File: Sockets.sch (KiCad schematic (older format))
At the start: 55 parts, among them J10 CA58SUB-B, J11 PC6 EPSON MAINBOARD, J12 Y AXIS, J13 Z AXIS, J14 LED 1, J15 LED 2, J6 LIMIT Y BACK, J7 LIMIT Y FRONT, J8 LIMIT Z UP, J9 LIMIT Z DOWN, Q1 2N7002K, Q2 2N7002K, Q3 2N7002K, Q4 2N7002K, Q5 2N7002K, Q6 2N7002K, Q7 2N7002K, U5 74HC245

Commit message: Routing almost finished
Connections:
- net LED1_CNT: now also RN1.1 (R1.1); no longer RN2.4 (R4.1)
- net LED1_CONTROL: now also U5.5 (A3); no longer U5.6 (A4)
- net LED2_CNT: now also RN1.2 (R2.1); no longer RN2.3 (R3.1)
- net LED2_CONTROL: now also U5.4 (A2); no longer U5.7 (A5)
- net SPI_MOSI: now also U5.2 (A0); no longer U5.8 (A6)
- net SPI_MOSI_BUF: now also RN1.4 (R4.1); no longer RN2.2 (R2.1)
- net SPI_SCLK: now also U5.3 (A1); no longer U5.9 (A7)
- net SPI_SCLK_BUF: now also RN1.3 (R3.1); no longer RN2.1 (R1.1)
- net YDIR: now also RN2.2 (R2.1); no longer RN1.3 (R3.1)
- net YSTEP: now also RN2.1 (R1.1); no longer RN1.4 (R4.1)
- net Y_DIR: now also U5.8 (A6); no longer U5.3 (A1)
- net Y_STEP: now also U5.9 (A7); no longer U5.2 (A0)
- net ZDIR: now also RN2.4 (R4.1); no longer RN1.1 (R1.1)
- net ZSTEP: now also RN2.3 (R3.1); no longer RN1.2 (R2.1)
- net Z_DIR: now also U5.6 (A4); no longer U5.5 (A3)
- net Z_STEP: now also U5.7 (A5); no longer U5.4 (A2)
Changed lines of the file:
@@
 Text Notes 4550 2600 0    50   ~ 0
 PE Signal Output to Emulate PE Sensor
-Text GLabel 4700 5600 0    50   Input ~ 0
+Text GLabel 4700 6300 0    50   Input ~ 0
 Y_STEP
-Text GLabel 4700 5700 0    50   Input ~ 0
+Text GLabel 4700 6200 0    50   Input ~ 0
 Y_DIR
+Text GLabel 4700 6100 0    50   Input ~ 0
+Z_STEP
+Text GLabel 4700 6000 0    50   Input ~ 0
+Z_DIR
+Text GLabel 4700 5900 0    50   Input ~ 0
+LED1_CONTROL
 Text GLabel 4700 5800 0    50   Input ~ 0
-Z_STEP
-Text GLabel 4700 5900 0    50   Input ~ 0
-Z_DIR
-Text GLabel 4700 6000 0    50   Input ~ 0
-LED1_CONTROL
-Text GLabel 4700 6100 0    50   Input ~ 0
 LED2_CONTROL
 $Comp
@@
 Wire Wire Line
 	4550 6500 4700 6500
-Text Label 6550 5600 2    50   ~ 0
+Text Label 6550 6300 2    50   ~ 0
 YSTEP
-Text Label 6550 5700 2    50   ~ 0
+Text Label 6550 6200 2    50   ~ 0
 YDIR
+Text Label 6550 6100 2    50   ~ 0
+ZSTEP
+Text Label 6550 6000 2    50   ~ 0
+ZDIR
+Text Label 6550 5900 2    50   ~ 0
+LED1_CNT
 Text Label 6550 5800 2    50   ~ 0
-ZSTEP
-Text Label 6550 5900 2    50   ~ 0
-ZDIR
-Text Label 6550 6000 2    50   ~ 0
-LED1_CNT
-Text Label 6550 6100 2    50   ~ 0
 LED2_CNT
 Text Label 7700 5050 2    50   ~ 0
@@
 	5700 6300 5750 6300
 Wire Wire Line
-	6150 5600 6550 5600
+	6150 6300 6550 6300
 Wire Wire Line
-	6150 5700 6550 5700
+	6150 6200 6550 6200
+Wire Wire Line
+	6150 6100 6550 6100
+Wire Wire Line
+	6150 6000 6550 6000
 Wire Wire Line
 	6150 5800 6550 5800
 Wire Wire Line
 	6150 5900 6550 5900
-Wire Wire Line
-	6150 6000 6550 6000
-Wire Wire Line
-	6150 6100 6550 6100
 Wire Notes Line
 	4050 4450 6750 4450
@@
 Text Notes 7500 2650 0    50   ~ 0
 Optional Step/DIR Outputs
-Text GLabel 4700 6300 0    50   Input ~ 0
+Text GLabel 4700 5700 0    50   Input ~ 0
 SPI_SCLK
-Text GLabel 4700 6200 0    50   Input ~ 0
+Text GLabel 4700 5600 0    50   Input ~ 0
 SPI_MOSI
-Text GLabel 6150 6200 2    50   Output ~ 0
+Text GLabel 6150 5600 2    50   Output ~ 0
 SPI_MOSI_BUF
-Text GLabel 6150 6300 2    50   Output ~ 0
+Text GLabel 6150 5700 2    50   Output ~ 0
 SPI_SCLK_BUF
 Wire Wire Line

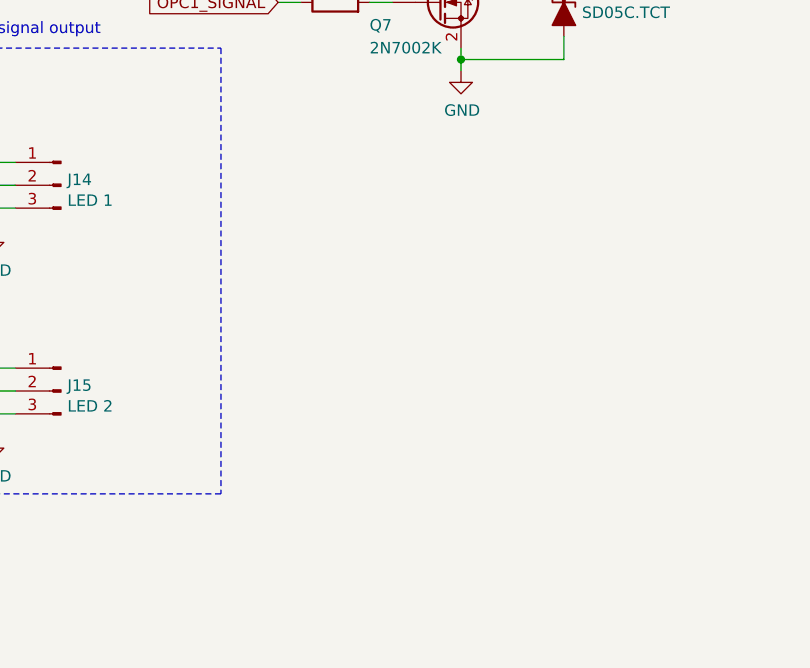
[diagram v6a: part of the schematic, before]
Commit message: Test points, start power plane routing, little change on schematic
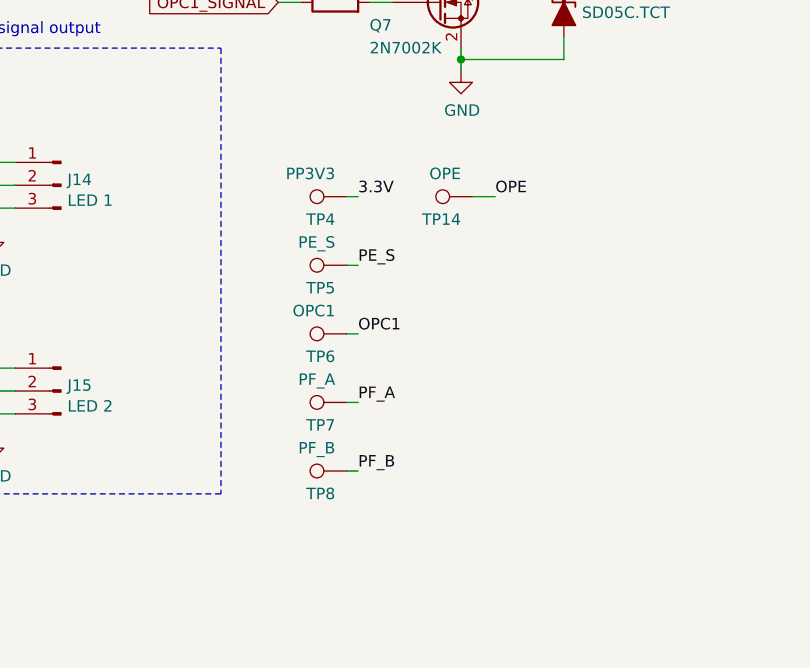
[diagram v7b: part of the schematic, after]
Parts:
- added TP14: OPE, TestPoint:TestPoint_Pad_D1.5mm, symbol Connector:TestPoint
- added TP4: PP3V3, TestPoint:TestPoint_Pad_D1.5mm, symbol Connector:TestPoint
- added TP5: PE_S, TestPoint:TestPoint_Pad_D1.5mm, symbol Connector:TestPoint
- added TP6: OPC1, TestPoint:TestPoint_Pad_D1.5mm, symbol Connector:TestPoint
- added TP7: PF_A, TestPoint:TestPoint_Pad_D1.5mm, symbol Connector:TestPoint
- added TP8: PF_B, TestPoint:TestPoint_Pad_D1.5mm, symbol Connector:TestPoint
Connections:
- net 3.3V: now also TP4.1
- net OPC1: now also TP6.1
- net OPE: now also TP14.1
- net PE_S: now also TP5.1
- net PF_A: now also TP7.1
- net PF_B: now also TP8.1
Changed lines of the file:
@@
 Text Label 10250 3550 0    50   ~ 0
 3.3V
+$Comp
+L Connector:TestPoint TP?
+U 1 1 5E2CDFFB
+P 9750 5100
+AR Path="/5DE588DC/5E2CDFFB" Ref="TP?"  Part="1"
+AR Path="/5DE587B9/5E2CDFFB" Ref="TP?"  Part="1"
+AR Path="/5E1018C2/5E2CDFFB" Ref="TP?"  Part="1"
+AR Path="/5DFB2EC0/5E2CDFFB" Ref="TP?"  Part="1"
+AR Path="/5E07245F/5E2CDFFB" Ref="TP4"  Part="1"
+F 0 "TP4" V 9650 5150 50  0000 L CNN
+F 1 "PP3V3" V 9850 5150 50  0000 L CNN
+F 2 "TestPoint:TestPoint_Pad_D1.5mm" H 9950 5100 50  0001 C CNN
+F 3 "~" H 9950 5100 50  0001 C CNN
+	1    9750 5100
+	0    -1   -1   0
+$EndComp
+$Comp
+L Connector:TestPoint TP?
+U 1 1 5E2D6BD7
+P 9750 5400
+AR Path="/5DE588DC/5E2D6BD7" Ref="TP?"  Part="1"
+AR Path="/5DE587B9/5E2D6BD7" Ref="TP?"  Part="1"
+AR Path="/5E1018C2/5E2D6BD7" Ref="TP?"  Part="1"
+AR Path="/5DFB2EC0/5E2D6BD7" Ref="TP?"  Part="1"
+AR Path="/5E07245F/5E2D6BD7" Ref="TP5"  Part="1"
+F 0 "TP5" V 9650 5450 50  0000 L CNN
+F 1 "PE_S" V 9850 5450 50  0000 L CNN
+F 2 "TestPoint:TestPoint_Pad_D1.5mm" H 9950 5400 50  0001 C CNN
+F 3 "~" H 9950 5400 50  0001 C CNN
+	1    9750 5400
+	0    -1   -1   0
+$EndComp
+$Comp
+L Connector:TestPoint TP?
+U 1 1 5E2D6DDE
+P 9750 5700
+AR Path="/5DE588DC/5E2D6DDE" Ref="TP?"  Part="1"
+AR Path="/5DE587B9/5E2D6DDE" Ref="TP?"  Part="1"
+AR Path="/5E1018C2/5E2D6DDE" Ref="TP?"  Part="1"
+AR Path="/5DFB2EC0/5E2D6DDE" Ref="TP?"  Part="1"
+AR Path="/5E07245F/5E2D6DDE" Ref="TP6"  Part="1"
+F 0 "TP6" V 9650 5750 50  0000 L CNN
+F 1 "OPC1" V 9850 5750 50  0000 L CNN
+F 2 "TestPoint:TestPoint_Pad_D1.5mm" H 9950 5700 50  0001 C CNN
+F 3 "~" H 9950 5700 50  0001 C CNN
+	1    9750 5700
+	0    -1   -1   0
+$EndComp
+$Comp
+L Connector:TestPoint TP?
+U 1 1 5E2D7B97
+P 9750 6000
+AR Path="/5DE588DC/5E2D7B97" Ref="TP?"  Part="1"
+AR Path="/5DE587B9/5E2D7B97" Ref="TP?"  Part="1"
+AR Path="/5E1018C2/5E2D7B97" Ref="TP?"  Part="1"
+AR Path="/5DFB2EC0/5E2D7B97" Ref="TP?"  Part="1"
+AR Path="/5E07245F/5E2D7B97" Ref="TP7"  Part="1"
+F 0 "TP7" V 9650 6050 50  0000 L CNN
+F 1 "PF_A" V 9850 6050 50  0000 L CNN
+F 2 "TestPoint:TestPoint_Pad_D1.5mm" H 9950 6000 50  0001 C CNN
+F 3 "~" H 9950 6000 50  0001 C CNN
+	1    9750 6000
+	0    -1   -1   0
+$EndComp
+$Comp
+L Connector:TestPoint TP?
+U 1 1 5E2D7E85
+P 9750 6300
+AR Path="/5DE588DC/5E2D7E85" Ref="TP?"  Part="1"
+AR Path="/5DE587B9/5E2D7E85" Ref="TP?"  Part="1"
+AR Path="/5E1018C2/5E2D7E85" Ref="TP?"  Part="1"
+AR Path="/5DFB2EC0/5E2D7E85" Ref="TP?"  Part="1"
+AR Path="/5E07245F/5E2D7E85" Ref="TP8"  Part="1"
+F 0 "TP8" V 9650 6350 50  0000 L CNN
+F 1 "PF_B" V 9850 6350 50  0000 L CNN
+F 2 "TestPoint:TestPoint_Pad_D1.5mm" H 9950 6300 50  0001 C CNN
+F 3 "~" H 9950 6300 50  0001 C CNN
+	1    9750 6300
+	0    -1   -1   0
+$EndComp
+$Comp
+L Connector:TestPoint TP?
+U 1 1 5E2D80F3
+P 10300 5100
+AR Path="/5DE588DC/5E2D80F3" Ref="TP?"  Part="1"
+AR Path="/5DE587B9/5E2D80F3" Ref="TP?"  Part="1"
+AR Path="/5E1018C2/5E2D80F3" Ref="TP?"  Part="1"
+AR Path="/5DFB2EC0/5E2D80F3" Ref="TP?"  Part="1"
+AR Path="/5E07245F/5E2D80F3" Ref="TP14"  Part="1"
+F 0 "TP14" V 10200 5150 50  0000 L CNN
+F 1 "OPE" V 10400 5150 50  0000 L CNN
+F 2 "TestPoint:TestPoint_Pad_D1.5mm" H 10500 5100 50  0001 C CNN
+F 3 "~" H 10500 5100 50  0001 C CNN
+	1    10300 5100
+	0    -1   -1   0
+$EndComp
+Text Label 10400 5100 0    50   ~ 0
+OPE
+Wire Wire Line
+	10300 5100 10400 5100
+Text Label 9800 5100 0    50   ~ 0
+3.3V
+Wire Wire Line
+	9750 5100 9800 5100
+Text Label 9800 5400 0    50   ~ 0
+PE_S
+Wire Wire Line
+	9750 5400 9800 5400
+Text Label 9800 5700 0    50   ~ 0
+OPC1
+Wire Wire Line
+	9750 5700 9800 5700
+Text Label 9800 6000 0    50   ~ 0
+PF_A
+Wire Wire Line
+	9750 6000 9800 6000
+Text Label 9800 6300 0    50   ~ 0
+PF_B
+Wire Wire Line
+	9750 6300 9800 6300
 $EndSCHEMATC

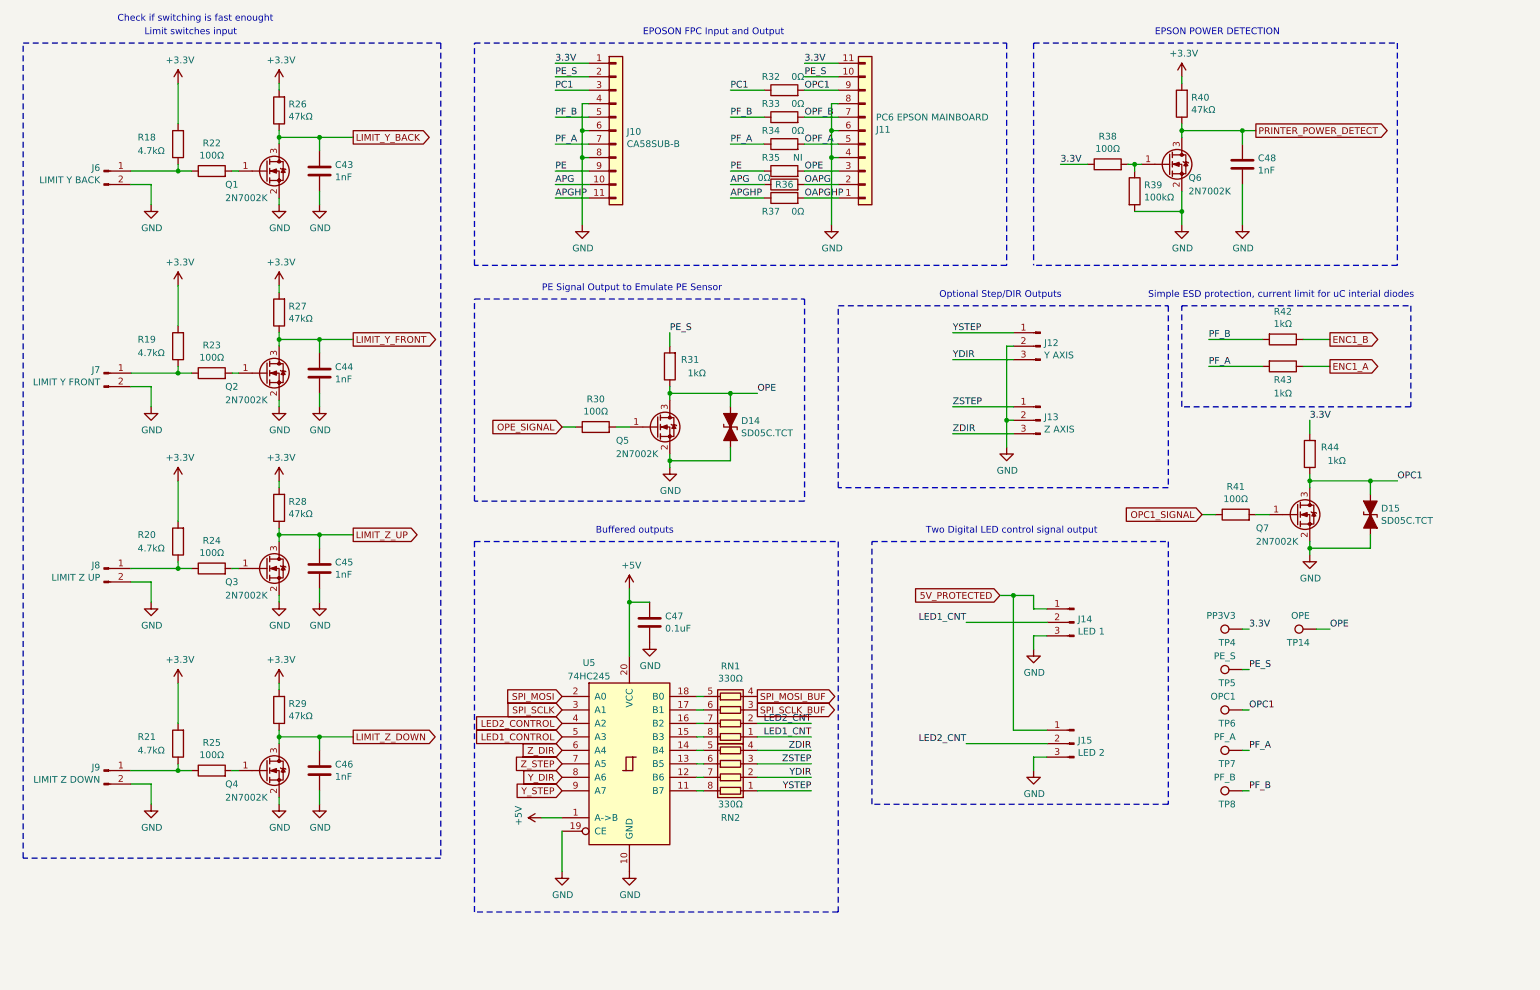
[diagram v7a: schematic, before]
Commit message: Update elements value
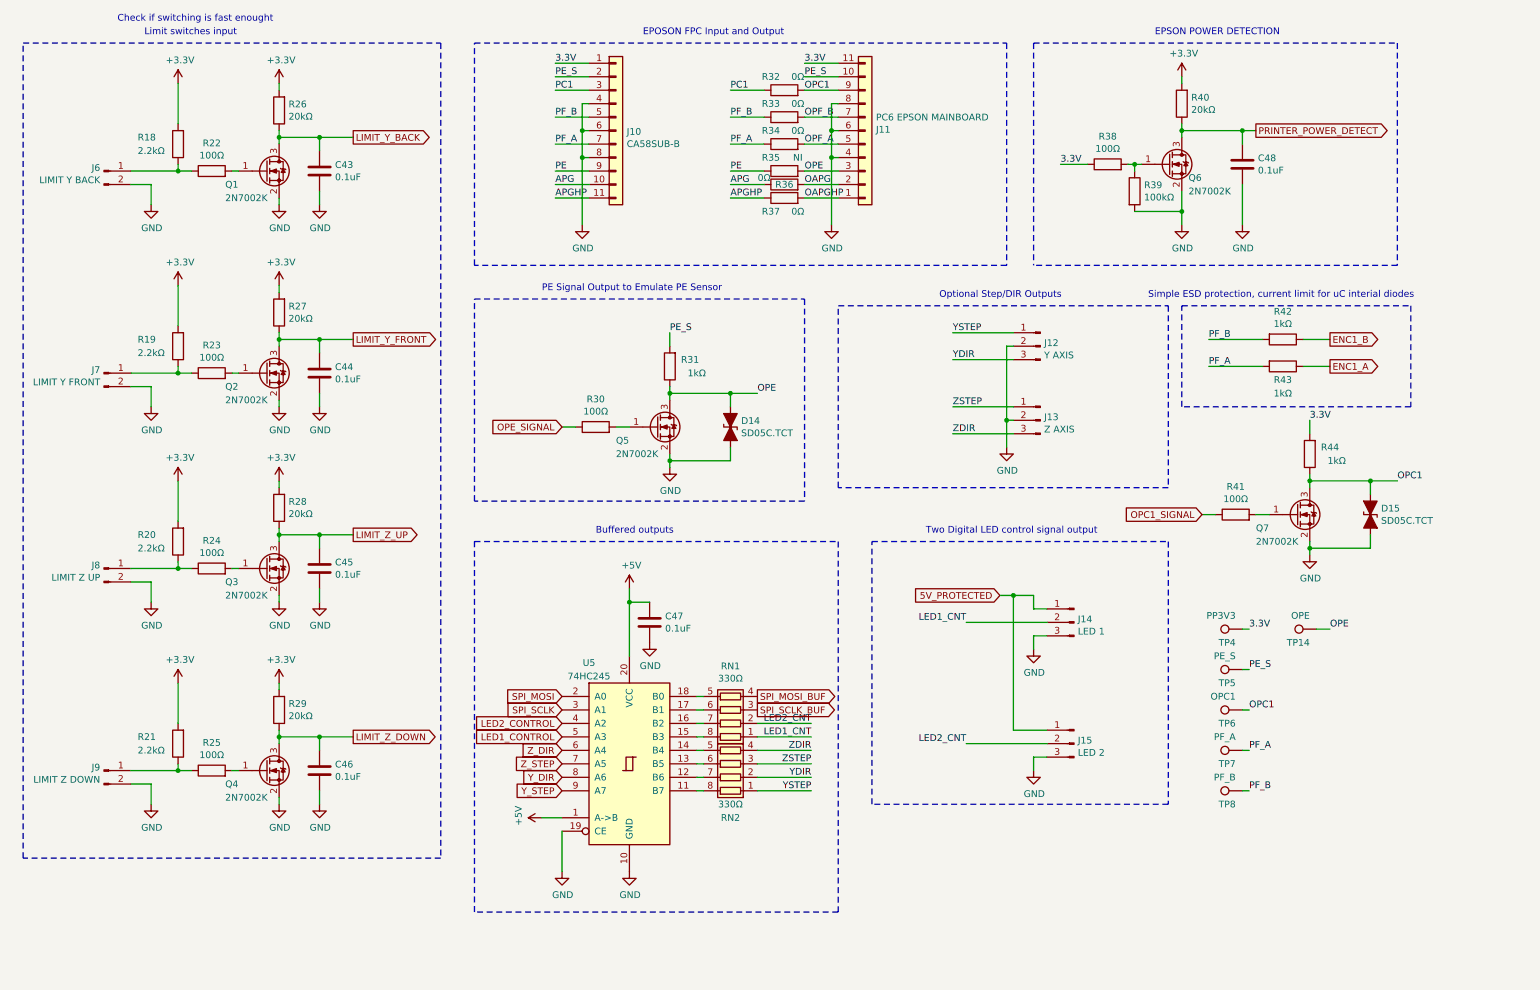
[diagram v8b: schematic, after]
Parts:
- C43, C44, C45, C46, C48: value 1nF -> 0.1uF
- R18, R19, R20, R21: value 4.7kΩ -> 2.2kΩ
- R22, R23, R24, R25, R30, R38, R41: Cena (none) -> 0.03185; Link (none) -> https://www.tme.eu/pl/details/smd0603-100r-1%25/rezystory-s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; Model (none) -> 0603SAF1000T5E; Opis (none) -> Rezystor: thick film; SMD; 0603; 100Ω; 0,1W; ±1%; -55÷155°C; Producent (none) -> ROYAL OHM; Typ (none) -> SMD
- R26, R27, R28, R29, R40: value 47kΩ -> 20kΩ; Cena (none) -> 0.03572; Link (none) -> https://www.tme.eu/pl/details/smd0603-47k/rezystory-smd-060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; Model (none) -> 0603SAJ0473T5E; Opis (none) -> Rezystor: thick film; SMD; 0603; 47kΩ; 0,1W; ±5%; -55÷155°C; Producent (none) -> ROYAL OHM; Typ (none) -> SMD
- R35: Cena 0.04651 -> (none)
- R39: Cena (none) -> 0.04651
